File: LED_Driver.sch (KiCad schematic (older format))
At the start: 0 parts

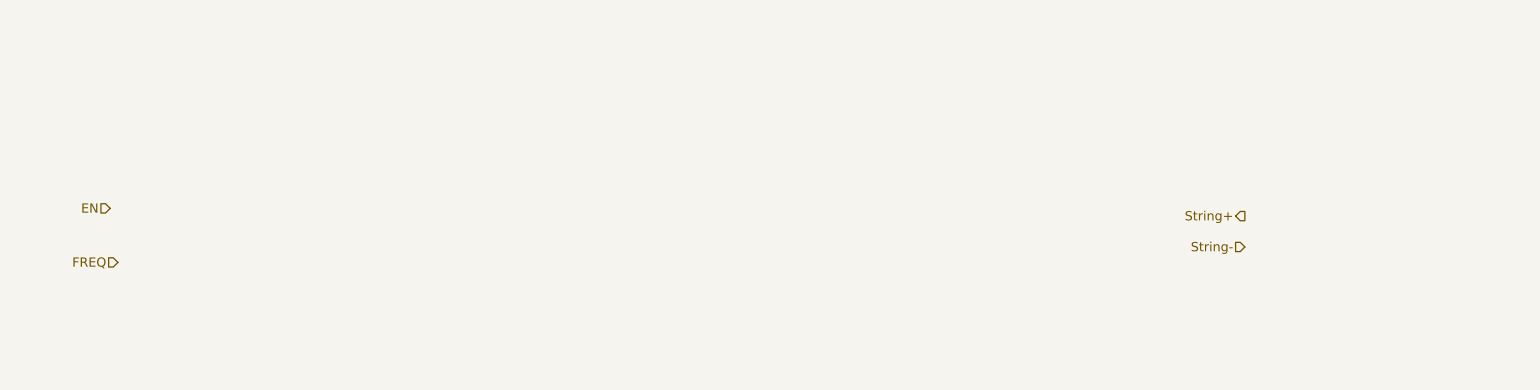
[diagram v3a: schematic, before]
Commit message: Module 3, Unit 8: Understanding The LED Driver Module
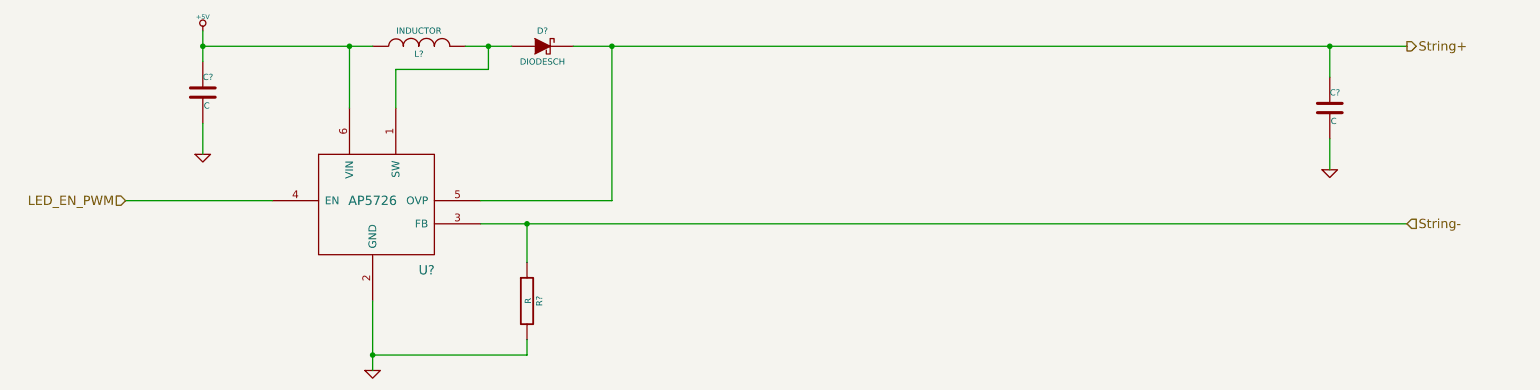
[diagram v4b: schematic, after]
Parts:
- added C? (x2): C, symbol C
- added D?: DIODESCH, symbol DIODESCH
- added L?: INDUCTOR, symbol INDUCTOR
- added R?: R, symbol R
- added U?: AP5726, symbol AP5726
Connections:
- net String+: now also C?.1, D?.2 (K), U?.5 (OVP)
- net String-: now also R?.1, U?.3 (FB)
- new net: D?.1 (A), L?.2, U?.1 (SW)
- new net +5V: C?.1, L?.1, U?.6 (VIN)
- new net GND: C?.2, C?.2, R?.2, U?.2 (GND)
- new net LED_EN_PWM: U?.4 (EN)
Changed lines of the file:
@@
 $Descr A4 11693 8268
 encoding utf-8
-Sheet 6 9
+Sheet 7 9
 Title ""
 Date ""
@@
 Comment4 ""
 $EndDescr
-Text HLabel 2000 2350 0    60   Input ~ 0
-EN
-Text HLabel 2050 2700 0    60   Input ~ 0
-FREQ
-Text HLabel 9350 2400 0    60   Output ~ 0
+Text HLabel 2100 2300 0    60   Input ~ 0
+LED_EN_PWM
+Text HLabel 10400 1300 2    60   Output ~ 0
 String+
-Text HLabel 9350 2600 0    60   Input ~ 0
+Text HLabel 10400 2450 2    60   Input ~ 0
 String-
+$Comp
+L AP5726 U?
+U 1 1 5301A60A
+P 3700 2300
+F 0 "U?" H 4050 1850 60  0000 C CNN
+F 1 "AP5726" H 3700 2300 60  0000 C CNN
+F 2 "" H 3700 2300 60  0000 C CNN
+F 3 "" H 3700 2300 60  0000 C CNN
+	1    3700 2300
+	1    0    0    -1
+$EndComp
+Wire Wire Line
+	2100 2300 3050 2300
+$Comp
+L +5V #PWR?
+U 1 1 5301A9B4
+P 2600 1200
+F 0 "#PWR?" H 2600 1290 20  0001 C CNN
+F 1 "+5V" H 2600 1290 30  0000 C CNN
+F 2 "" H 2600 1200 60  0000 C CNN
+F 3 "" H 2600 1200 60  0000 C CNN
+	1    2600 1200
+	1    0    0    -1
+$EndComp
+$Comp
+L GND #PWR?
+U 1 1 5301A9C8
+P 2600 2000
+F 0 "#PWR?" H 2600 2000 30  0001 C CNN
+F 1 "GND" H 2600 1930 30  0001 C CNN
+F 2 "" H 2600 2000 60  0000 C CNN
+F 3 "" H 2600 2000 60  0000 C CNN
+	1    2600 2000
+	1    0    0    -1
+$EndComp
+$Comp
+L GND #PWR?
+U 1 1 5301A9DA
+P 3700 3400
+F 0 "#PWR?" H 3700 3400 30  0001 C CNN
+F 1 "GND" H 3700 3330 30  0001 C CNN
+F 2 "" H 3700 3400 60  0000 C CNN
+F 3 "" H 3700 3400 60  0000 C CNN
+	1    3700 3400
+	1    0    0    -1
+$EndComp
+$Comp
+L C C?
+U 1 1 5301A9E7
+P 2600 1600
+F 0 "C?" H 2600 1700 40  0000 L CNN
+F 1 "C" H 2606 1515 40  0000 L CNN
+F 2 "" H 2638 1450 30  0000 C CNN
+F 3 "" H 2600 1600 60  0000 C CNN
+	1    2600 1600
+	1    0    0    -1
+$EndComp
+Wire Wire Line
+	2600 1800 2600 2000
+Wire Wire Line
+	2600 1200 2600 1400
+Wire Wire Line
+	2600 1300 3700 1300
+Wire Wire Line
+	3550 1300 3550 1700
+Connection ~ 2600 1300
+$Comp
+L C C?
+U 1 1 5301AA06
+P 9900 1700
+F 0 "C?" H 9900 1800 40  0000 L CNN
+F 1 "C" H 9906 1615 40  0000 L CNN
+F 2 "" H 9938 1550 30  0000 C CNN
+F 3 "" H 9900 1700 60  0000 C CNN
+	1    9900 1700
+	1    0    0    -1
+$EndComp
+$Comp
+L INDUCTOR L?
+U 1 1 5301AA1A
+P 4000 1300
+F 0 "L?" V 3950 1300 40  0000 C CNN
+F 1 "INDUCTOR" V 4100 1300 40  0000 C CNN
+F 2 "" H 4000 1300 60  0000 C CNN
+F 3 "" H 4000 1300 60  0000 C CNN
+	1    4000 1300
+	0    -1   -1   0
+$EndComp
+Connection ~ 3550 1300
+Wire Wire Line
+	3850 1700 3850 1450
+Wire Wire Line
+	3850 1450 4450 1450
+Wire Wire Line
+	4450 1450 4450 1300
+Wire Wire Line
+	4300 1300 4600 1300
+$Comp
+L DIODESCH D?
+U 1 1 5301AA4D
+P 4800 1300
+F 0 "D?" H 4800 1400 40  0000 C CNN
+F 1 "DIODESCH" H 4800 1200 40  0000 C CNN
+F 2 "" H 4800 1300 60  0000 C CNN
+F 3 "" H 4800 1300 60  0000 C CNN
+	1    4800 1300
+	1    0    0    -1
+$EndComp
+Connection ~ 4450 1300
+Wire Wire Line
+	5000 1300 10400 1300
+$Comp
+L GND #PWR?
+U 1 1 5301AA9E
+P 9900 2100
+F 0 "#PWR?" H 9900 2100 30  0001 C CNN
+F 1 "GND" H 9900 2030 30  0001 C CNN
+F 2 "" H 9900 2100 60  0000 C CNN
+F 3 "" H 9900 2100 60  0000 C CNN
+	1    9900 2100
+	1    0    0    -1
+$EndComp
+Wire Wire Line
+	9900 1500 9900 1300
+Connection ~ 9900 1300
+Wire Wire Line
+	9900 1900 9900 2100
+$Comp
+L R R?
+U 1 1 5301AAD4
+P 4700 2950
+F 0 "R?" V 4780 2950 40  0000 C CNN
+F 1 "R" V 4707 2951 40  0000 C CNN
+F 2 "" V 4630 2950 30  0000 C CNN
+F 3 "" H 4700 2950 30  0000 C CNN
+	1    4700 2950
+	1    0    0    -1
+$EndComp
+Wire Wire Line
+	3700 2950 3700 3400
+Wire Wire Line
+	4700 3200 4700 3300
+Wire Wire Line
+	4700 3300 3700 3300
+Connection ~ 3700 3300
+Wire Wire Line
+	4700 2700 4700 2450
+Wire Wire Line
+	4400 2450 10400 2450
+Connection ~ 4700 2450
+Wire Wire Line
+	4400 2300 5250 2300
+Wire Wire Line
+	5250 2300 5250 1300
+Connection ~ 5250 1300
 $EndSCHEMATC

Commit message: Module 3, Unit 9: Understanding The Arduino Module
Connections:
- net String+ renamed LED_STRING+
- net String- renamed LED_STRING-
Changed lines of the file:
@@
 LED_EN_PWM
 Text HLabel 10400 1300 2    60   Output ~ 0
-String+
-Text HLabel 10400 2450 2    60   Input ~ 0
-String-
+LED_STRING+
+Text HLabel 10400 2450 2    60   Output ~ 0
+LED_STRING-
 $Comp
 L AP5726 U?
